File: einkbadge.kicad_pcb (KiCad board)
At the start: 2 copper layers, 108.2 x 99.1 mm, 427 parts, among them J1 USB_C_Receptacle_USB2.0_14P, J2 Conn_01x03, J3 Conn_01x14_Pin, J4 Conn_01x16_Pin, J5 Conn_01x03_Pin, J6 Conn_01x03_Pin, Q1 Si1308EDL, SW1 SW_Push, SW2 SW_Push, SW3 SW_Push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

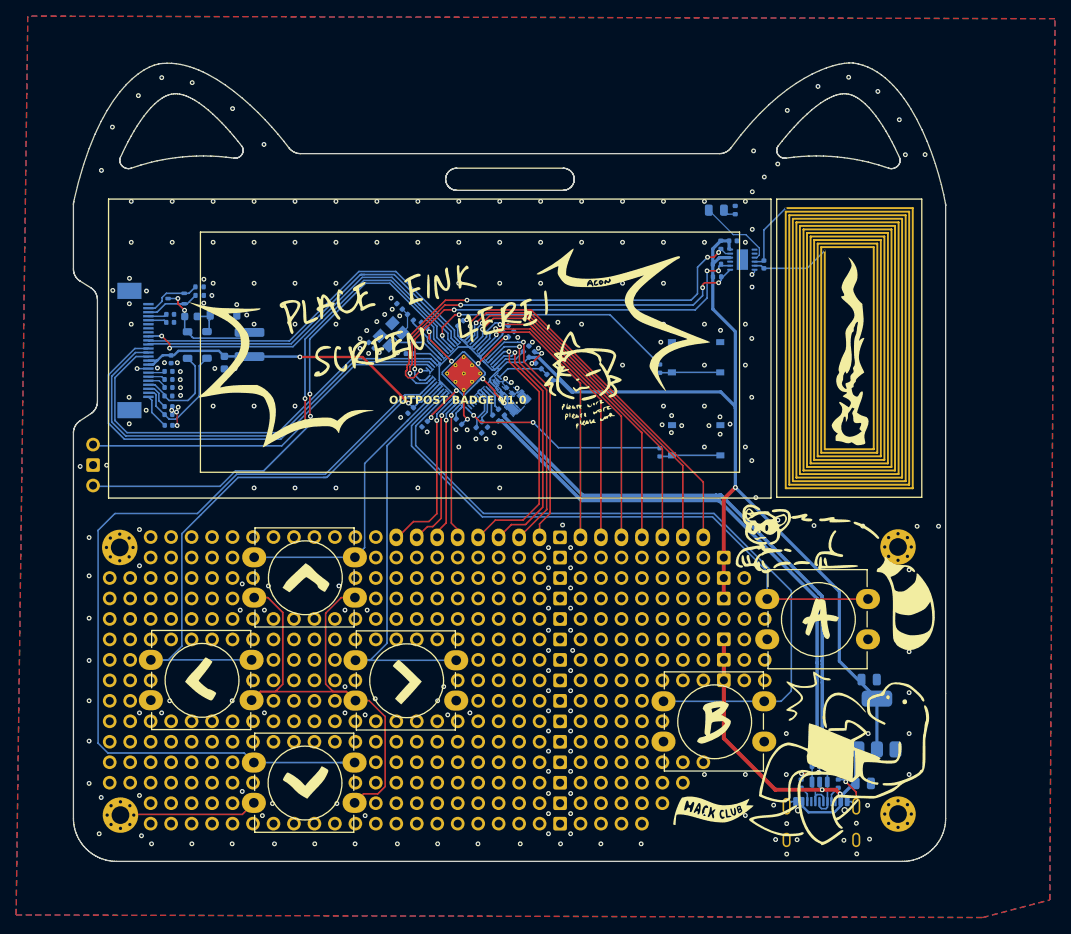
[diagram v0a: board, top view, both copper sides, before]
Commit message: Update silkscreen, soldermask and MPNs
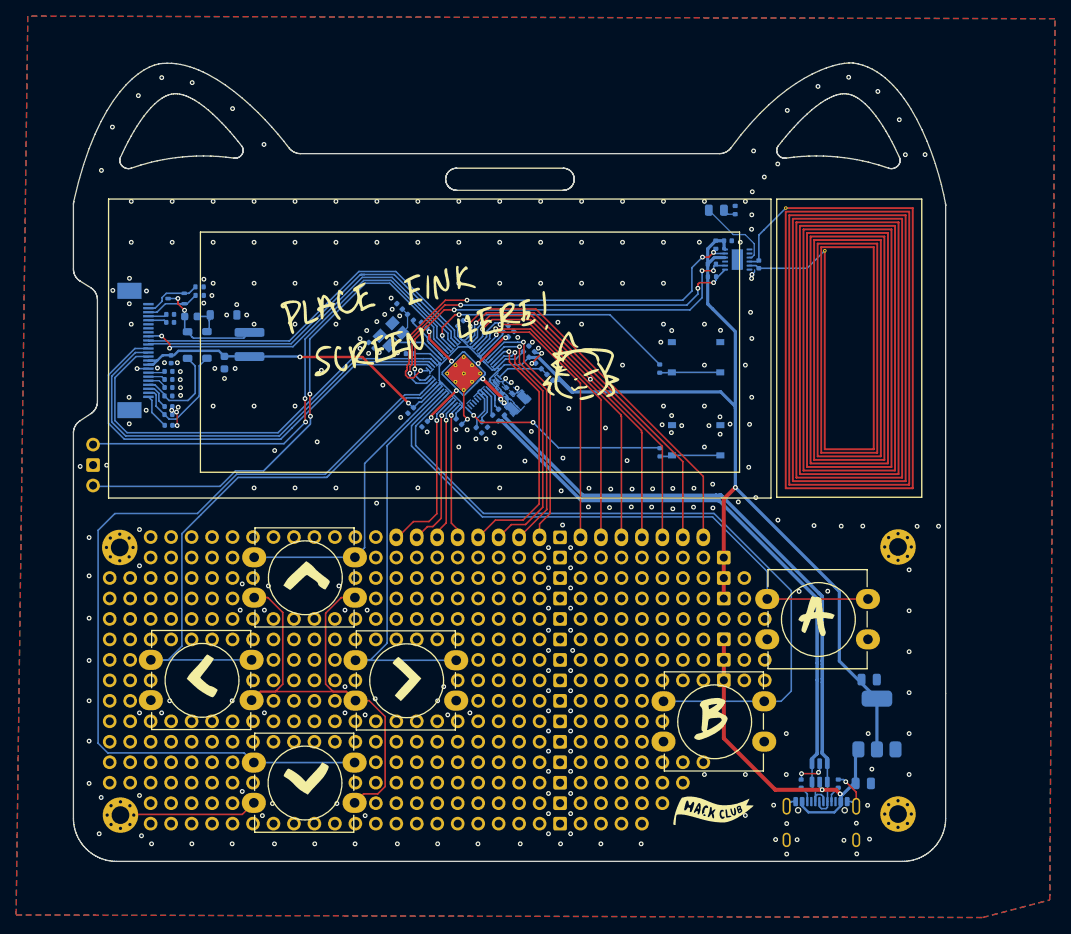
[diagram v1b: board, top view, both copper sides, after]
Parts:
- removed the G*** at (228.3, 114.1) (x2)
- removed the G*** at (201.1, 119.5)
- added G*** (x2): LOGO, LOGO, F.Cu at (227.9, 114.0)
- added G*** (x2): LOGO, LOGO, B.Cu at (204.2, 119.4)
- R6: value 1K -> 1k
- moved C22 0.63 mm to (231.5, 86.2)
- moved C23 0.63 mm to (235.3, 89.1)
- moved R11 0.63 mm to (229.5, 90.6)
- moved R14 0.63 mm to (230.0, 86.7)
- moved R9 0.63 mm to (229.5, 89.1)
- moved U4 0.63 mm to (232.7, 88.5)
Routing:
- net +1V1: track 51.0 -> 55.7 mm
- net PUSH_3: track 110.3 -> 108.6 mm
- net GND: track 109.4 -> 108.6 mm, vias 275 -> 307
- net 2: track 0.00 -> 0.73 mm, vias 0 -> 1
- net NFC_SDA: track 52.1 -> 51.3 mm
- net Net-(U4-AC1): track 9.75 -> 10.4 mm
- net NFC_SCL: track 53.5 -> 52.9 mm
- net /GPIO19: track 47.5 -> 48.0 mm
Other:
- board text removed: "OUTPOST BADGE V1.0"

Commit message: Fix bad git merge
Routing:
- net 2: track 0.73 -> 0.00 mm, vias 1 -> 0
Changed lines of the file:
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@@
 	)
 	(via
-		(at 234.5 90.36)
-		(size 0.6)
-		(drill 0.3)
-		(layers "F.Cu" "B.Cu")
-		(net 2)
-	)
-	(via
 		(at 182.88 86.36)
 		(size 0.6)
@@
 	)
 	(segment
-		(start 234.8225 89.759999)
-		(end 234.8225 90.0375)
-		(width 0.15)
-		(layer "B.Cu")
-		(net 2)
-	)
-	(segment
 		(start 208.411679 100.131605)
 		(end 207.949083 100.131605)
@@
 	)
 	(segment
-		(start 234.8225 90.0375)
-		(end 234.5 90.36)
-		(width 0.15)
-		(layer "B.Cu")
-		(net 2)
-	)
-	(segment
